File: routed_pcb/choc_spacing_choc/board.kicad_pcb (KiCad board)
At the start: 2 copper layers, 100 x 100 mm, 28 parts

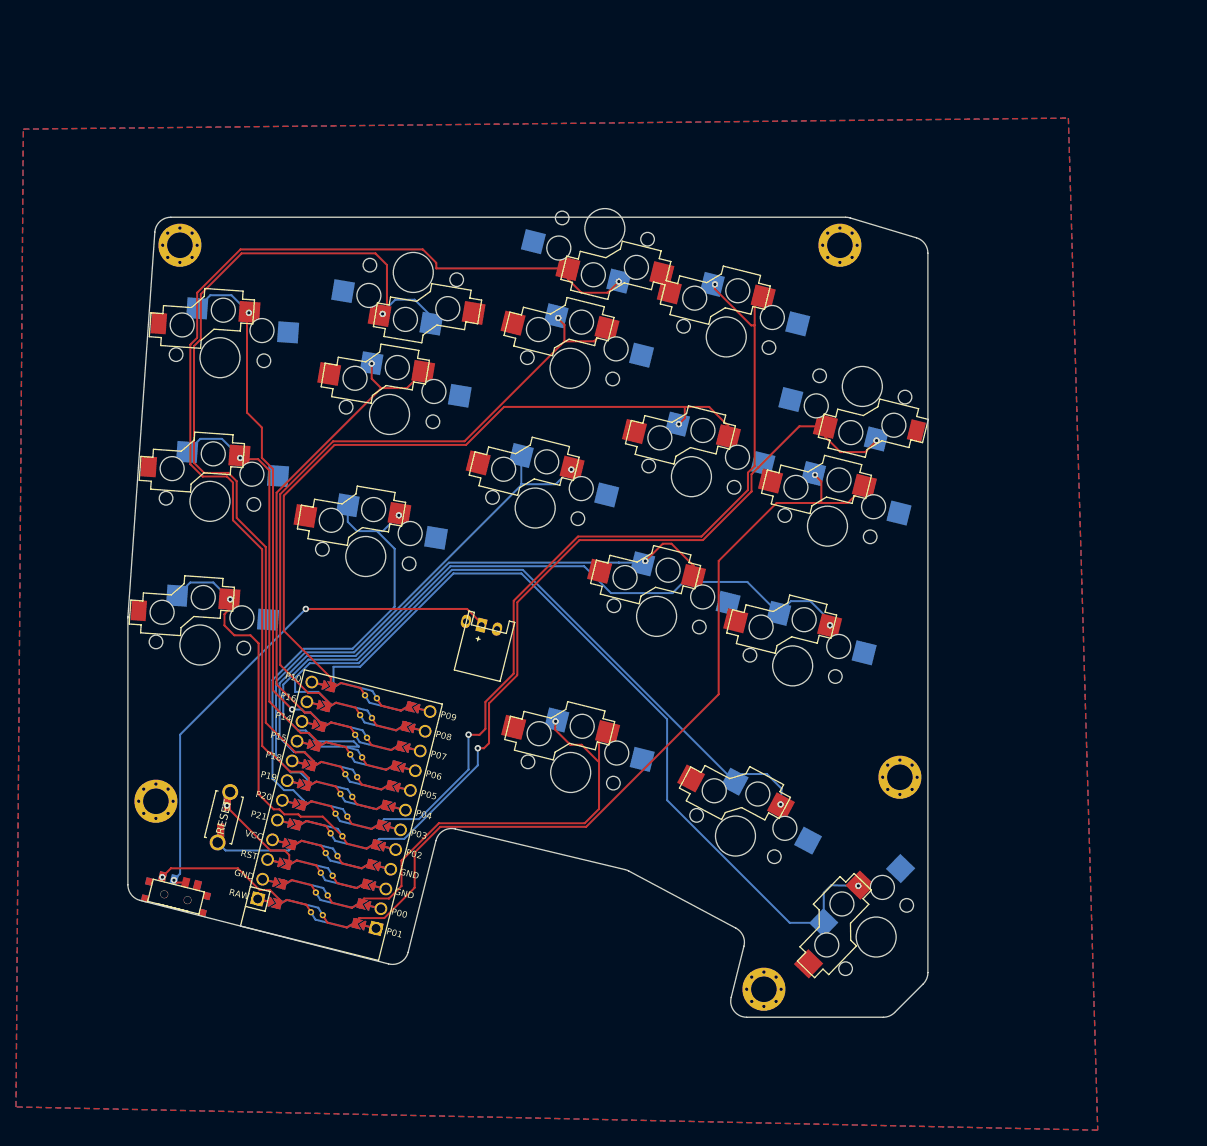
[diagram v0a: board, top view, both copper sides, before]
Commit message: choc v1.1 and mx v1.2
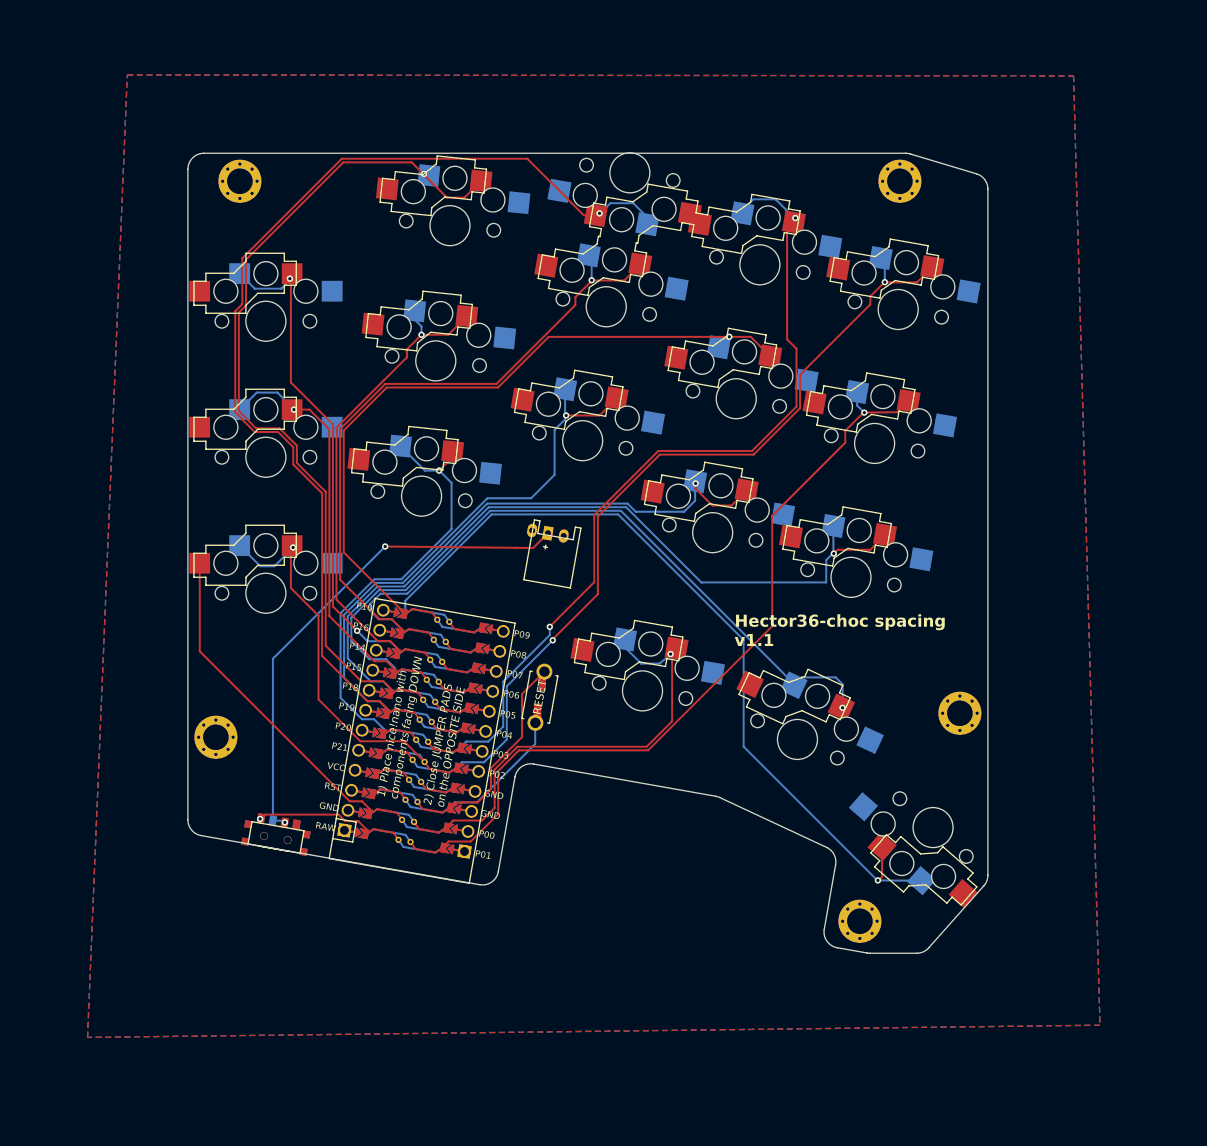
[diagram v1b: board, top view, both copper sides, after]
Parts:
- moved B1 42.3 mm to (131.5, 113.0), turned to -100 degrees
- moved B2 42.3 mm to (131.5, 113.0), turned to 80 degrees
- moved SW18 15.4 mm to (180.6, 129.3), turned to 139 degrees
- moved HOLE4 14.7 mm to (171.5, 141.0)
- moved T1 14.5 mm to (98.5, 130.6), turned to 170 degrees
- moved SW17 14.3 mm to (163.7, 118.3), turned to -25 degrees
- moved JST1 14.2 mm to (132.5, 92.5), turned to -10 degrees
- moved MCU1 13.7 mm to (117.0, 117.2), turned to 80 degrees
- moved SW16 13.6 mm to (144.3, 112.2), turned to -10 degrees
- moved SW13 13.3 mm to (170.4, 98.0), turned to -10 degrees
- moved SW10 12.6 mm to (153.1, 92.4), turned to -10 degrees
- moved SW14 11.9 mm to (173.3, 81.3), turned to -10 degrees
- moved SW11 11.2 mm to (156.0, 75.7), turned to -10 degrees
- moved HOLE1 11.0 mm to (94.0, 48.5)
- moved HOLE2 11.0 mm to (176.5, 48.5)
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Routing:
- net GND: track 10.3 -> 64.7 mm
- net matrix_ring_top: track 109.4 -> 103.0 mm
- net matrix_inner_home: track 102.5 -> 96.5 mm
- net matrix_inner_bottom: track 100.3 -> 94.5 mm
- net RST: track 11.9 -> 16.7 mm, vias 1 -> 0
- net matrix_index_top: track 106.0 -> 101.4 mm
- net thumb_tucky: track 87.7 -> 83.3 mm
- net matrix_index_home: track 91.5 -> 87.2 mm
- net matrix_ring_bottom: track 57.3 -> 53.6 mm
- net matrix_inner_top: track 98.0 -> 101.5 mm
- net matrix_pinky_bottom: track 49.3 -> 46.1 mm
- net matrix_middle_home: track 82.8 -> 79.7 mm
- net matrix_pinky_top: track 65.2 -> 62.6 mm
- net RAW: track 17.4 -> 15.1 mm
- net Bplus: track 65.3 -> 63.0 mm
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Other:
- outline, holes or cut-outs redrawn
- board text added: "1) Place nice!nano with components facing DOWN"
- board text added: "2) Close JUMPER PADS on the OPPOSITE SIDE"
- board text added: "Hector36-choc spacing v1.1"

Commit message: choc spacing v1.2 with all pads on bottom of key
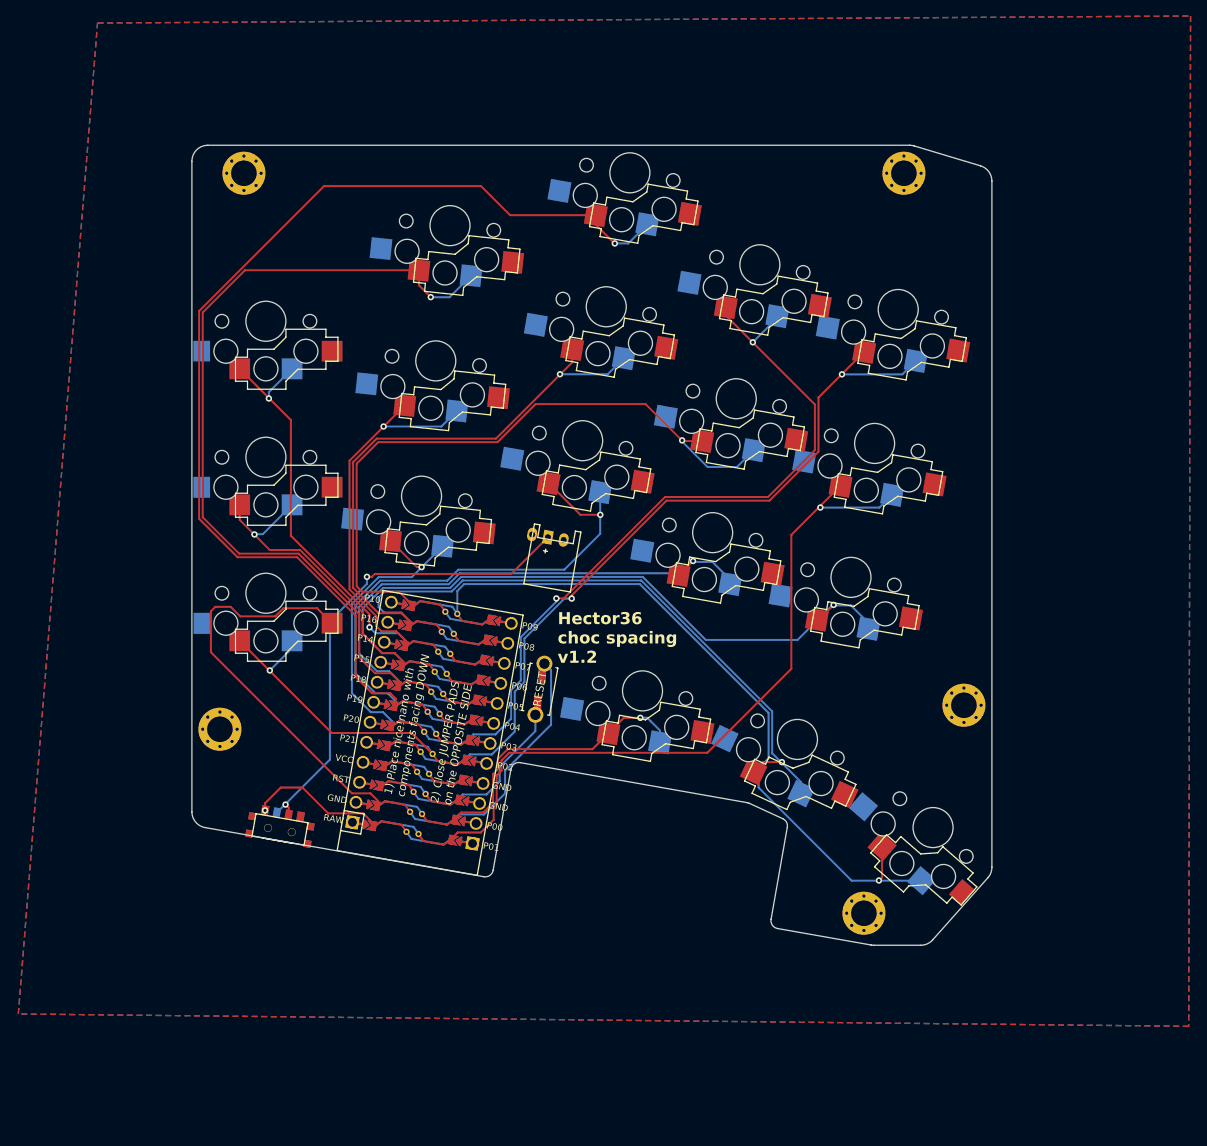
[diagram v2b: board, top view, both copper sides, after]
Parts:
- moved MCU1 1.41 mm to (118.0, 116.2)
- moved HOLE1 1.12 mm to (94.5, 47.5)
- moved HOLE2 1.12 mm to (177.0, 47.5)
- moved HOLE3 1.12 mm to (184.5, 114.0)
- moved HOLE4 1.12 mm to (172.0, 140.0)
- moved HOLE5 1.12 mm to (91.5, 117.0)
- moved T1 1.12 mm to (99.0, 129.6)
- moved B1 1.00 mm to (131.5, 112.0)
- moved B2 1.00 mm to (131.5, 112.0)
- moved JST1 0.50 mm to (132.5, 93.0)
- turned SW18 to -41 degrees
- turned SW9 to -10 degrees
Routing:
- net thumb_inner: track 54.0 -> 36.1 mm
- net matrix_ring_bottom: track 53.6 -> 37.8 mm
- net thumb_reachy: track 101.9 -> 88.3 mm
- net GND: track 64.7 -> 78.1 mm
- net matrix_pinky_top: track 62.6 -> 49.9 mm
- net matrix_middle_home: track 79.7 -> 68.2 mm
- net matrix_ring_home: track 58.4 -> 46.9 mm
- net matrix_pinky_bottom: track 46.1 -> 34.9 mm
- net matrix_pinky_home: track 49.0 -> 37.9 mm
- net matrix_index_top: track 101.4 -> 90.9 mm
- net matrix_inner_top: track 101.5 -> 91.3 mm
- net matrix_inner_bottom: track 94.5 -> 84.7 mm
- net matrix_index_bottom: track 74.4 -> 65.7 mm
- net matrix_inner_home: track 96.5 -> 90.4 mm
- net matrix_middle_bottom: track 67.7 -> 63.2 mm
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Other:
- outline, holes or cut-outs redrawn
- board text added: "Hector36 choc spacing v1.2"
- board text removed: "Hector36-choc spacing v1.1"
